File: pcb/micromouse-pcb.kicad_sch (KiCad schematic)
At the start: 39 parts, among them J1 Conn_01x08, J1_MotorEncoder1 Conn_01x06, J2 Conn_01x08, J2_MotorEncoder1 Conn_01x06, Q1 FQP27P06, SW3 SW_SPDT, SW6 SW_Push, U2 AP63205WU, U3 LSM6DSV16XTR, U4 DRV8833PW

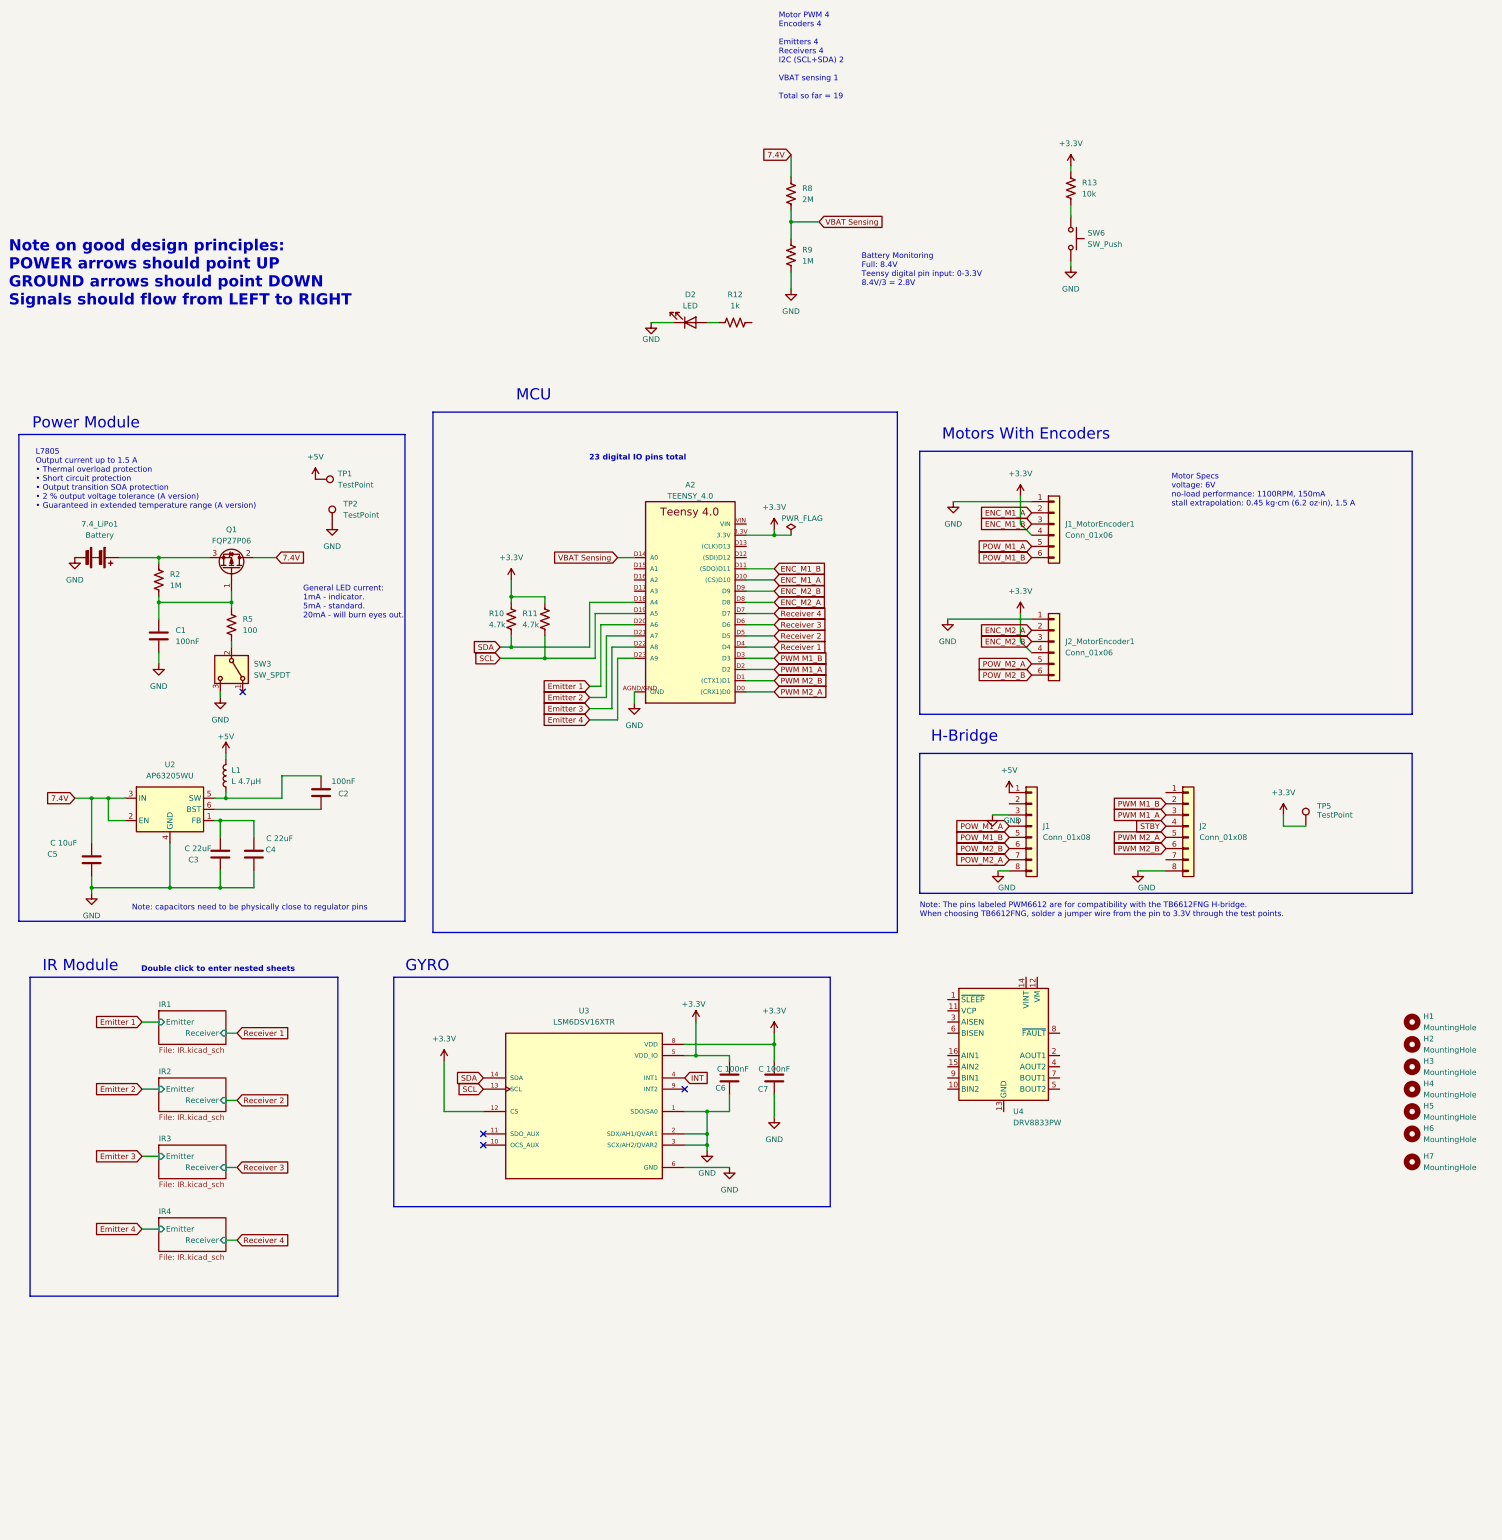
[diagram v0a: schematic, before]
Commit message: Did fan wiring
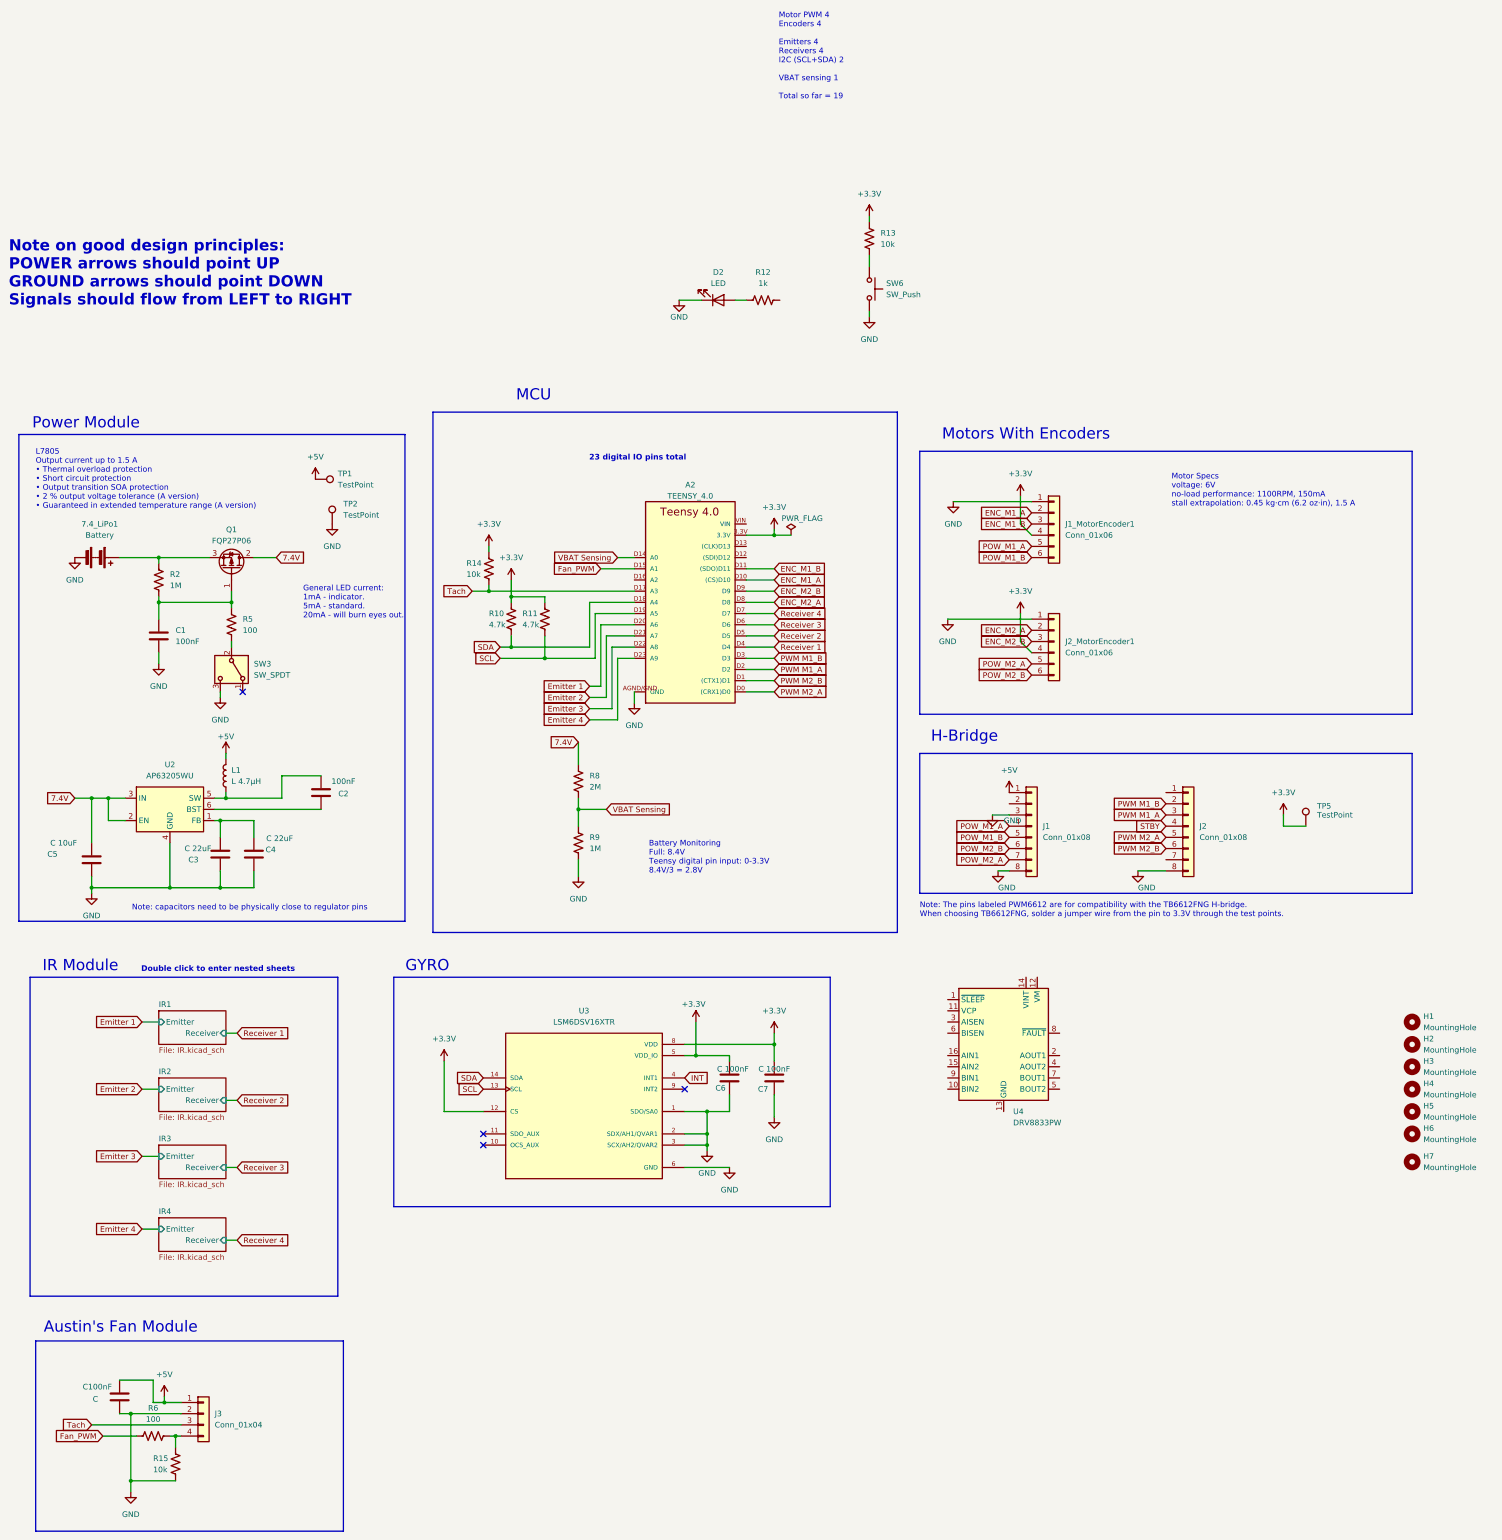
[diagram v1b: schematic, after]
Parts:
- added C100nF: C, symbol Device:C
- added J3: Conn_01x04, symbol Connector_Generic:Conn_01x04
- added R14, R15: 10k, Resistor_SMD:R_0603_1608Metric_Pad0.98x0.95mm_HandSolder, symbol Device:R_US
- added R6: 100, Resistor_SMD:R_0603_1608Metric_Pad0.98x0.95mm_HandSolder, symbol Device:R_US
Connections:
- net +3.3V: now also R14.1
- net +5V: now also C100nF.1, J3.1 (Pin_1)
- net GND: now also C100nF.2, J3.2 (Pin_2), R15.2
- net Fan_PWM: now reaches A2.D15 (A1)
- net Fan_PWM: now also R6.2
- net Tach: now reaches A2.D17 (A3)
- net Tach: now also J3.3 (Pin_3), R14.2
- new net: J3.4 (Pin_4), R15.1, R6.1
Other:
- note added: "Austin's Fan Module"
- moved on the sheet: D2, R12, R13, R8, R9, SW6
